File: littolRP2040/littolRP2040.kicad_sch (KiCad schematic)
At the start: 81 parts, among them J1 USB_C_Receptacle_USB2.0, J2 Conn_01x05, U1 SRV05-4, U2 XC6206PxxxMR, U3 W25Q128JVS, U4 RP2040, Y1 X322512MSB4SI

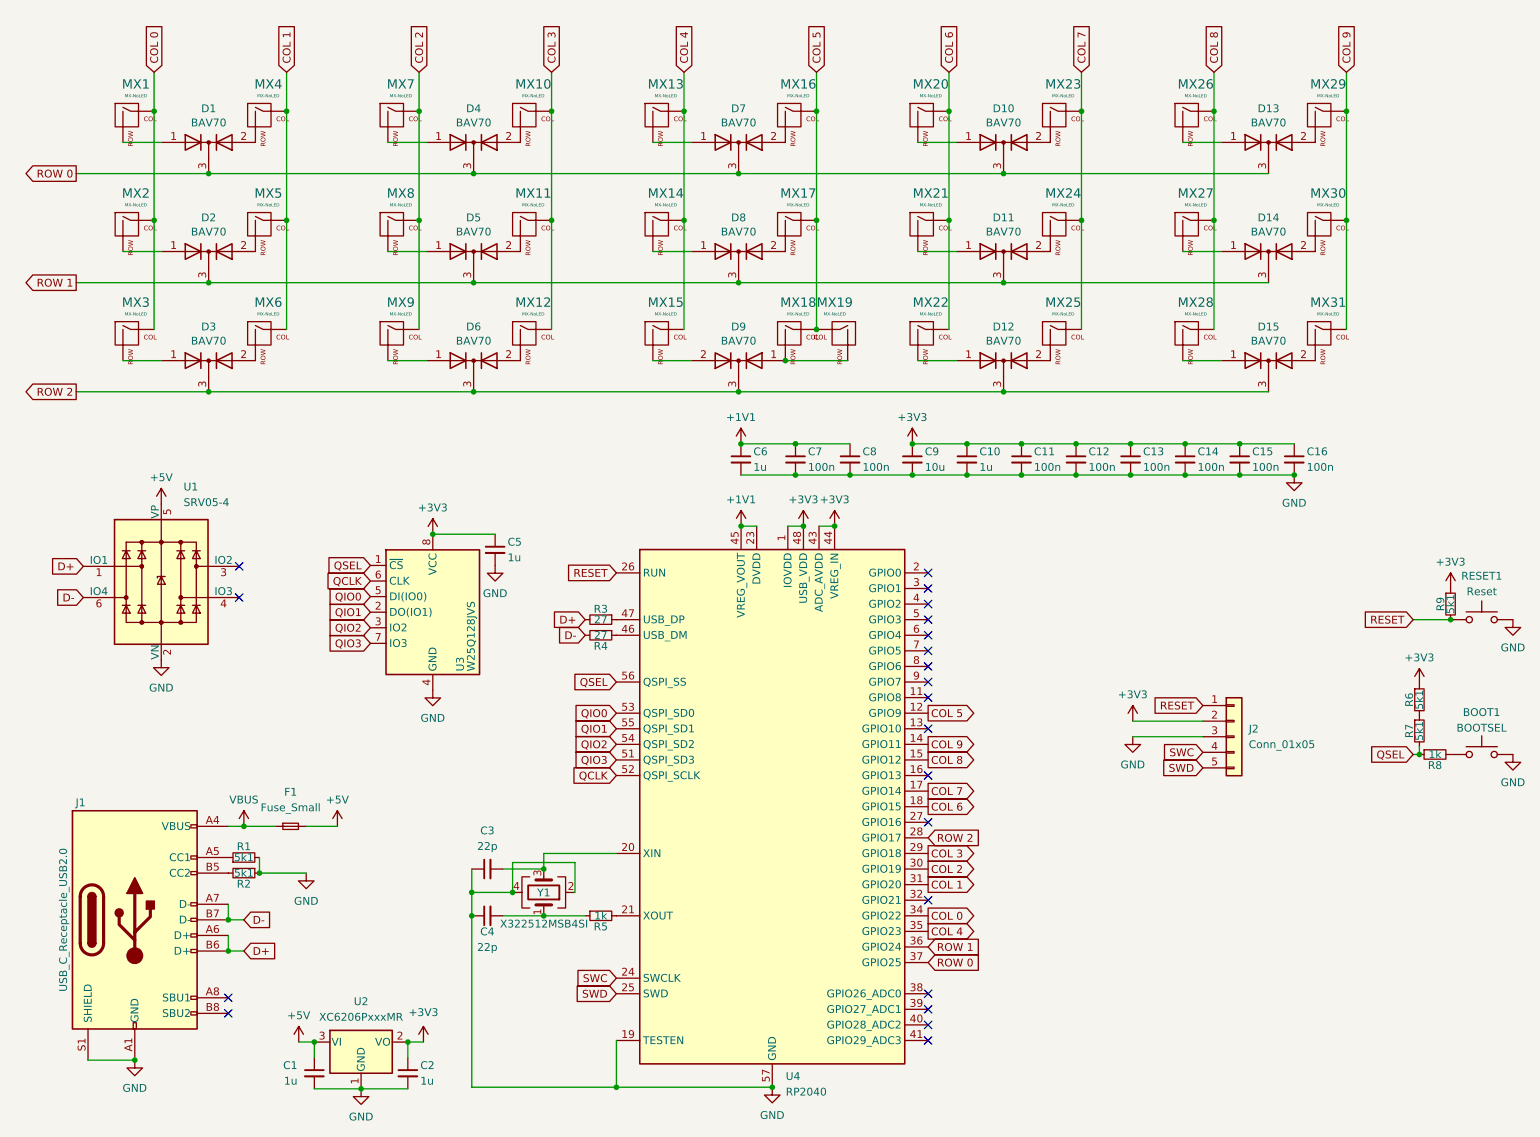
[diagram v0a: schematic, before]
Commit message: PCB cleanup. Updated fabrication files. Added BOM and position files for JLCPCB fabrication.
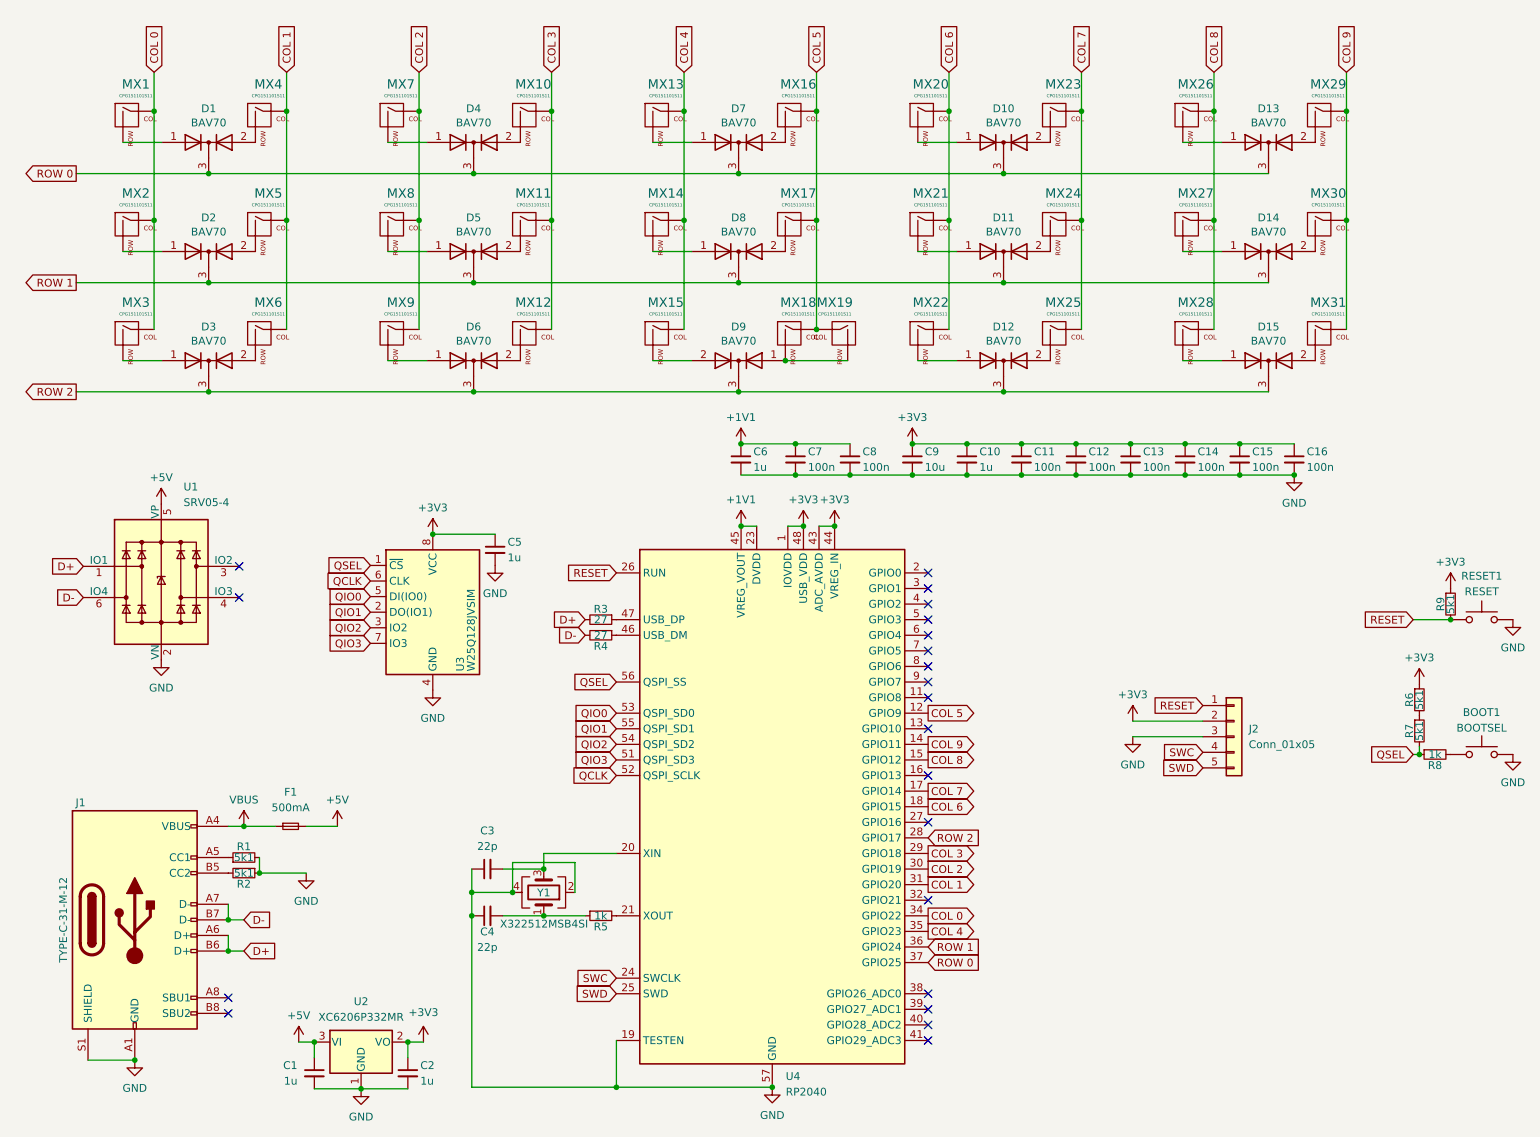
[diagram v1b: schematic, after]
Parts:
- BOOT1: LCSC (none) -> C318884
- C1, C10, C2, C5, C6: LCSC (none) -> C52923
- C11, C12, C13, C14, C15, C16, C7, C8: LCSC (none) -> C2655418
- C3, C4: LCSC (none) -> C1555
- C9: LCSC (none) -> C19702
- D1, D10, D11, D12, D13, D14, D15, D2, D3, D4, D5, D6, D7, D8, D9: LCSC (none) -> C2828461
- F1: value Fuse_Small -> 500mA; LCSC (none) -> C377237
- J1: value USB_C_Receptacle_USB2.0 -> TYPE-C-31-M-12; LCSC (none) -> C165948
- J2: now left out of the parts list
- MX1, MX10, MX11, MX12, MX13, MX14, MX15, MX16, MX17, MX18, MX19, MX2, MX20, MX21, MX22, MX23, MX24, MX25, MX26, MX27, MX28, MX29, MX3, MX30, MX31, MX4, MX5, MX6, MX7, MX8, MX9: value MX-NoLED -> CPG151101S11; LCSC (none) -> C2803348
- R1, R2, R6, R7, R9: LCSC (none) -> C103086
- R3, R4: LCSC (none) -> C25100
- R5, R8: LCSC (none) -> C279987
- RESET1: value Reset -> RESET; LCSC (none) -> C318884
- U1: LCSC (none) -> C2972082
- U2: value XC6206PxxxMR -> XC6206P332MR; Field4 (none) -> C5446
- U3: value W25Q128JVS -> W25Q128JVSIM; LCSC (none) -> C2613930
- U4: LCSC (none) -> C2040
- Y1: LCSC (none) -> C9002
